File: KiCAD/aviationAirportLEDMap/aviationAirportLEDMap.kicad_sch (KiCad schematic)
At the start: 20 parts, among them J1 Screw_Terminal_01x03, J2 Screw_Terminal_01x03

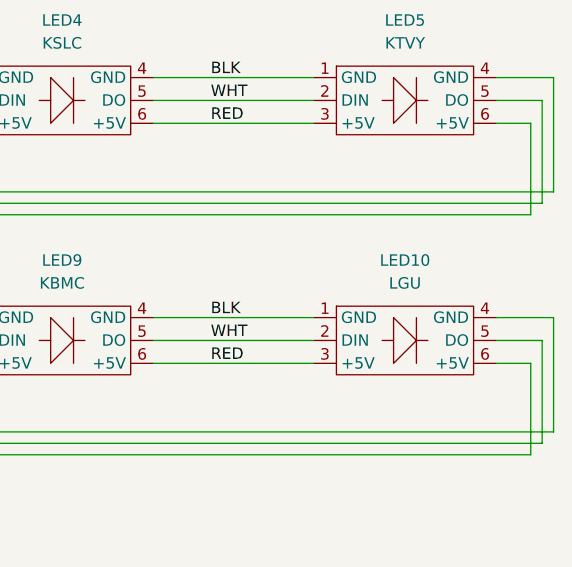
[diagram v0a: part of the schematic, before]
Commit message: added a method for flight catagory requests and decoding
just starting on main.

updated .gitignore to deal with more venv stuff and pycaches that show up.

added some requirements.txt dependencies.
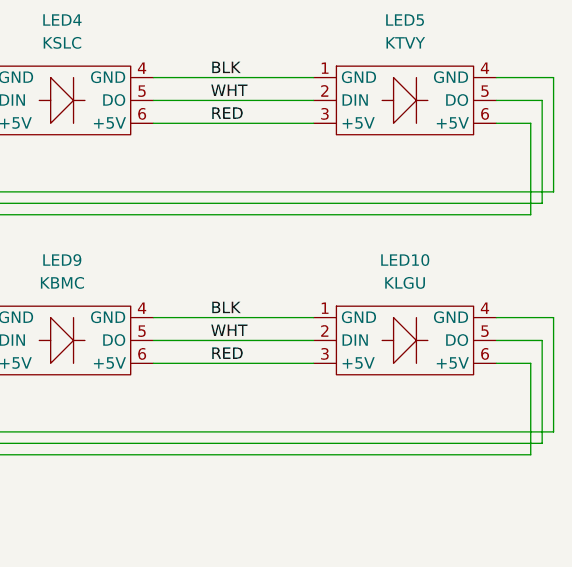
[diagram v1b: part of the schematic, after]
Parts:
- LED10: value LGU -> KLGU
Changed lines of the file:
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@@
 			)
 		)
-		(property "Value" "LGU"
+		(property "Value" "KLGU"
 			(at 392.43 78.74 0)
 			(show_name no)
